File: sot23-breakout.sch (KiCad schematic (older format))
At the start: 6 parts, among them J1 Conn_01x06, J2 Conn_01x06, Q1 Q_NMOS_GSD, Q2 Q_NMOS_GSD, Q3 Q_NMOS_GSD, Q4 Q_NMOS_GSD

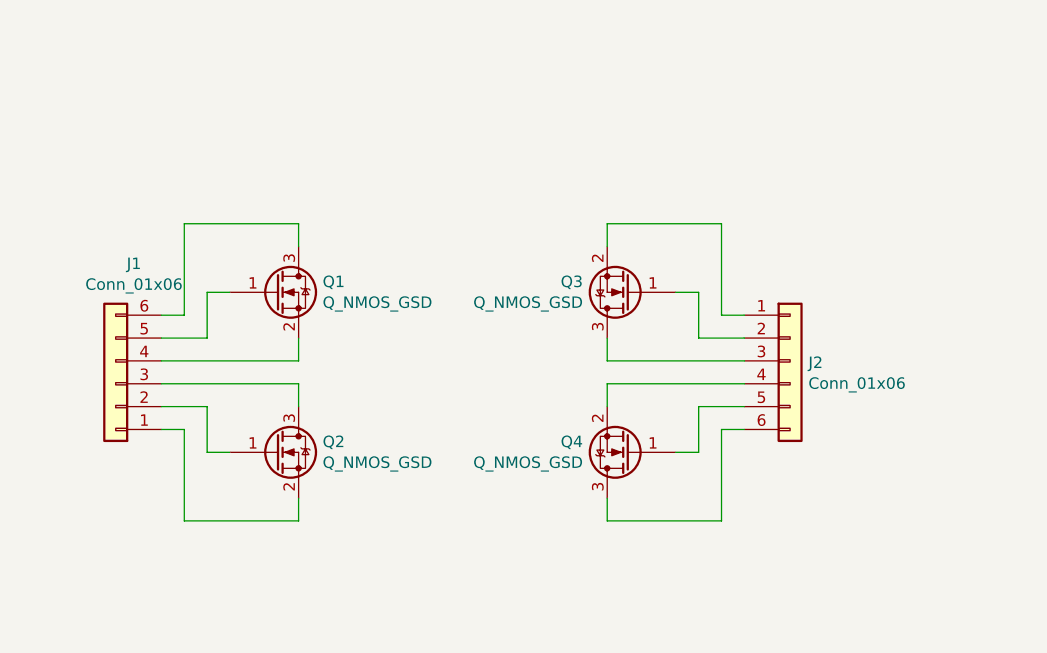
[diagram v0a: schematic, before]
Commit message: change SOT-23 breakout to have 8 chips
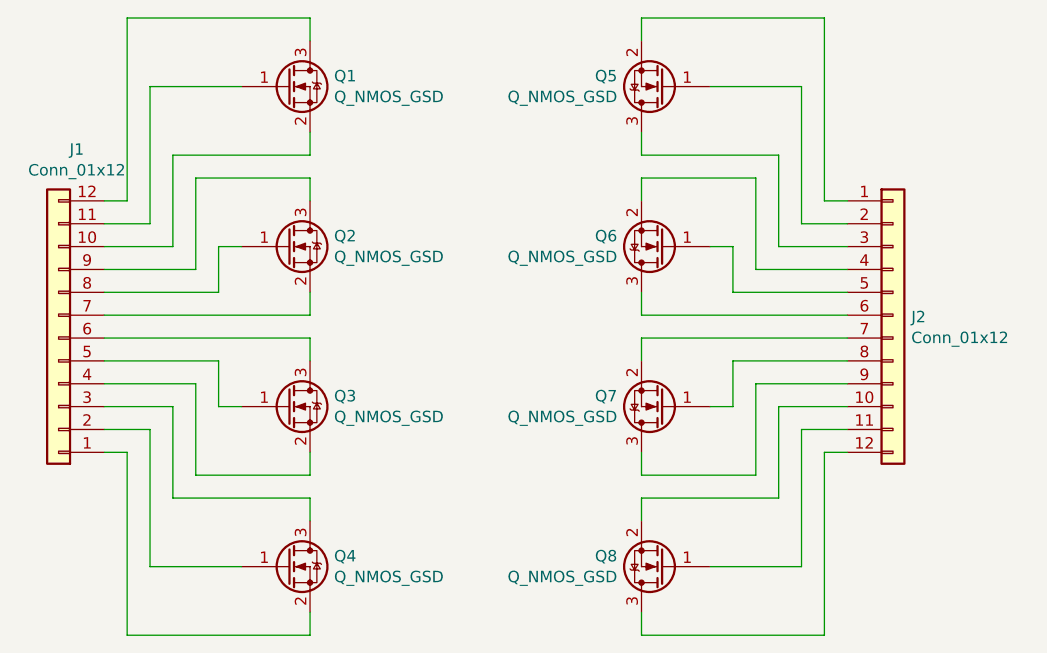
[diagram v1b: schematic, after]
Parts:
- removed J1, J2: Conn_01x06, footprints:Header_1x06_P2.54mm, symbol Connector_Generic:Conn_01x06
- added J1, J2: Conn_01x12, footprints:Header_1x12_P2.54mm, symbol Connector_Generic:Conn_01x12
- added Q3, Q4, Q7, Q8: Q_NMOS_GSD, Package_TO_SOT_SMD:SOT-23_Handsoldering, symbol Device:Q_NMOS_GSD
- renumbered Q3 to Q5, Q4 to Q6
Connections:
- net at Q5.2 (S): now also J2.1 (Pin_1)
- net at Q5.1 (G): now also J2.2 (Pin_2)
- net at Q5.3 (D): now also J2.3 (Pin_3)
- net at Q6.2 (S): now also J2.4 (Pin_4)
- net at Q6.1 (G): now also J2.5 (Pin_5)
- net at Q6.3 (D): now also J2.6 (Pin_6)
- net at Q2.2 (S): now also J1.7 (Pin_7)
- net at Q2.1 (G): now also J1.8 (Pin_8)
- net at Q2.3 (D): now also J1.9 (Pin_9)
- net at Q1.2 (S): now also J1.10 (Pin_10)
- net at Q1.1 (G): now also J1.11 (Pin_11)
- net at Q1.3 (D): now also J1.12 (Pin_12)
- new net: J2.8 (Pin_8), Q7.1 (G)
- new net: J2.7 (Pin_7), Q7.2 (S)
- new net: J2.9 (Pin_9), Q7.3 (D)
- new net: J2.10 (Pin_10), Q8.2 (S)
- new net: J2.11 (Pin_11), Q8.1 (G)
- new net: J2.12 (Pin_12), Q8.3 (D)
- new net: J1.2 (Pin_2), Q4.1 (G)
- new net: J1.1 (Pin_1), Q4.2 (S)
- new net: J1.3 (Pin_3), Q4.3 (D)
- new net: J1.5 (Pin_5), Q3.1 (G)
- new net: J1.4 (Pin_4), Q3.2 (S)
- new net: J1.6 (Pin_6), Q3.3 (D)
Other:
- moved on the sheet: Q5, Q6
